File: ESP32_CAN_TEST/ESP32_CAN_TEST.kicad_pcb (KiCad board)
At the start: 2 copper layers, 45.7 x 45.7 mm, 56 parts, among them J1 XT60, J2 Encoder_1, J3 Molex_2x2, J4 Encoder2, J5 i2C, J6 UART, J7 GH1.25, J8 Jack-DC, Q1 2N7002, Q2 2N7002, Q3 2N7002, Q4 2N7002, Q5 2N7002, Q6 2N7002, SW1 EN, SW2 EN, U1 AMS1117, U2 ESP32-WROOM-32, U3 AOZ1282CI, U4 SN65HVD230

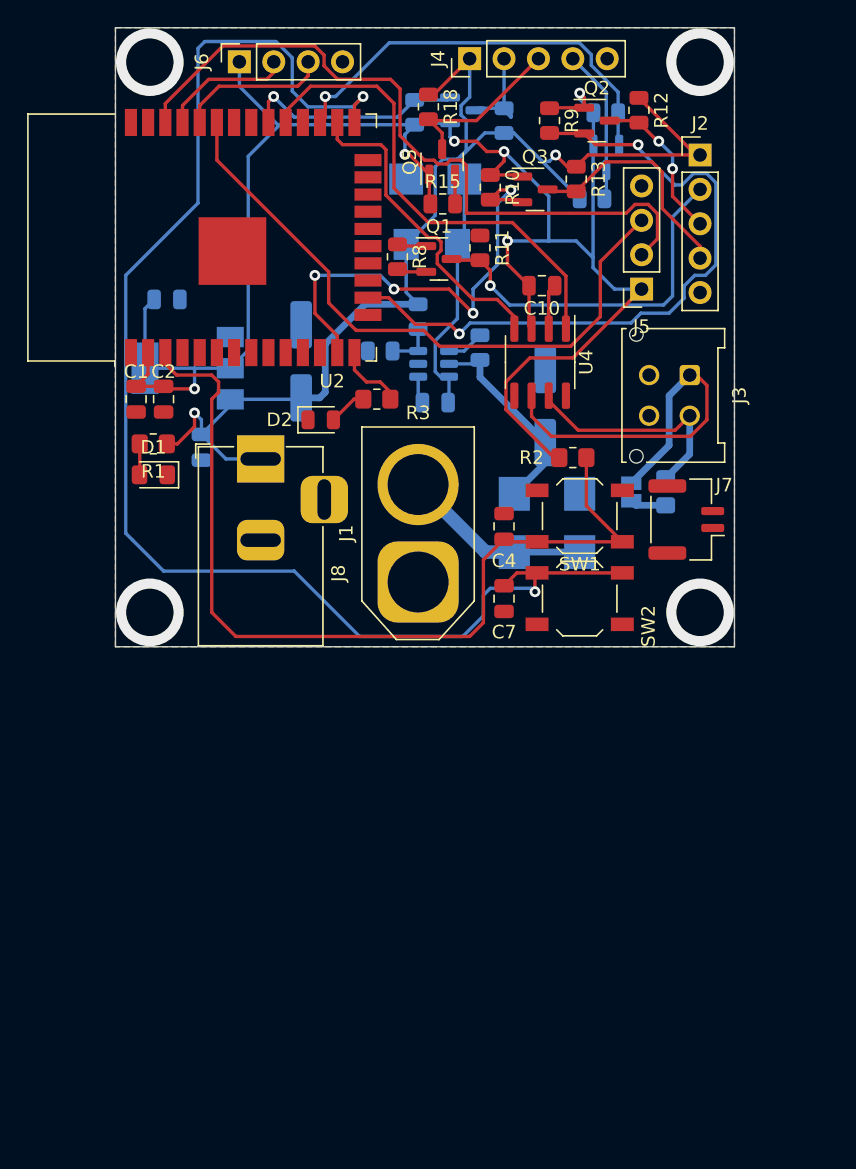
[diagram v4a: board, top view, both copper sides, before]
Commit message: esp32 fixed canbus
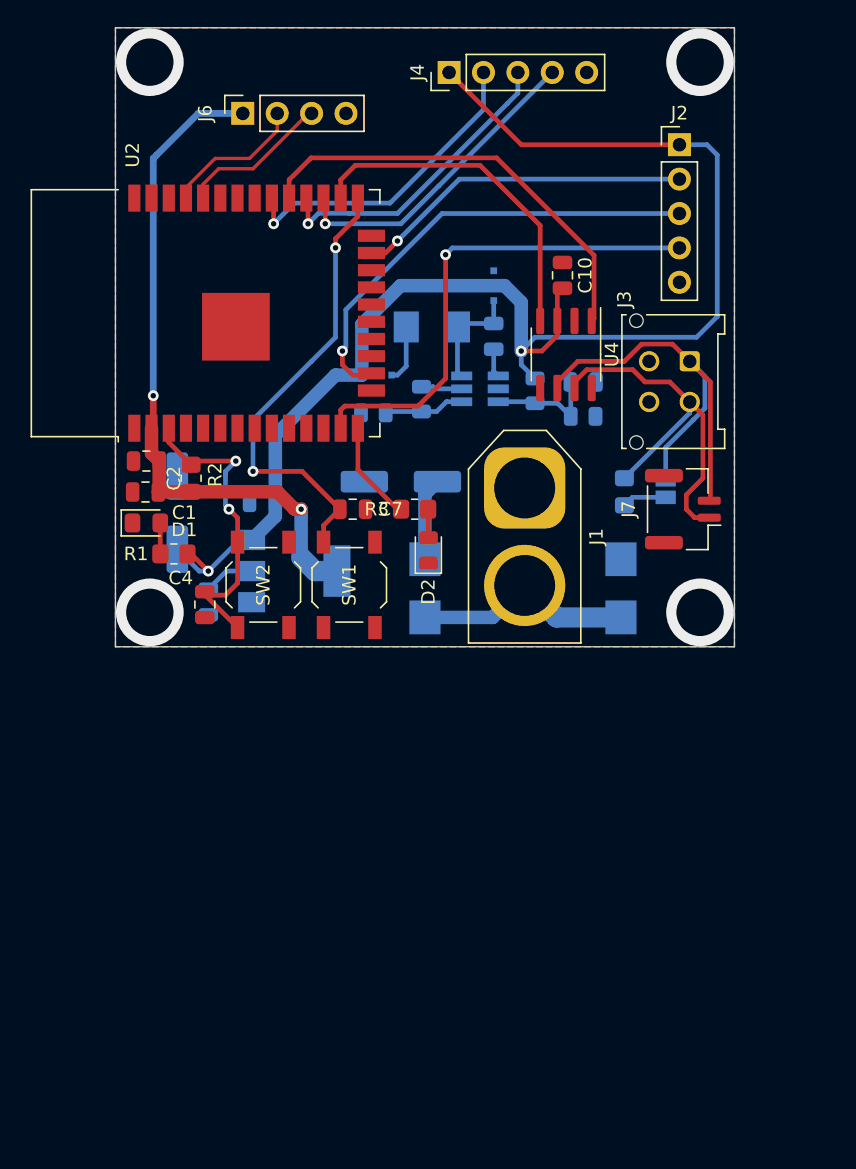
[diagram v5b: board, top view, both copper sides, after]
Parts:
- removed J5: i2C, Connector_PinSocket_2.54mm:PinSocket_1x04_P2.54mm_Vertical
- removed J8: Jack-DC, Connector_BarrelJack:BarrelJack_Horizontal
- removed Q1, Q2, Q3, Q4, Q5, Q6: 2N7002, Package_TO_SOT_SMD:SOT-23
- removed R10, R11, R12, R13, R14, R15, R16, R17, R18, R19, R9: 10K, Resistor_SMD:R_0805_2012Metric
- added C11: 100pF, Capacitor_SMD:C_0805_2012Metric, B.Cu at (136.1, 66.8)
- added D6: S4, Diode_SMD:D_SOD-323F, B.Cu at (129.5, 59.7)
- D5: value SS34 -> S4; footprint Diode_SMD:D_SMB -> Diode_SMD:D_SOD-323F
- L1: value 22uH -> 3.3uH
- R5: value 300K -> 27K
- R6: value 5.1k -> 22k
- R7: value 27K -> 124K
- R8: value 10K -> 2K2; moved to B.Cu
- U3: value AOZ1282CI -> MP2451; footprint Package_TO_SOT_SMD:SOT-23-6 -> Package_TO_SOT_SMD:SOT-23-6_Handsoldering
- U4: value SN65HVD230 -> TJA1051T
- moved R2 28.2 mm to (107.2, 73.9), turned to 90 degrees
- moved SW1 23.9 mm to (112.5, 81.8), turned to -90 degrees
- moved C4 22.8 mm to (108.2, 83.2), turned to -90 degrees
- moved C5 22.6 mm to (108.5, 83.1), turned to -90 degrees
- moved SW2 17.0 mm to (118.9, 81.8), turned to 90 degrees
- moved U1 16.9 mm to (114.8, 80.8), turned to 0 degrees
- moved R6 15.7 mm to (136.1, 69.3), turned to 0 degrees
- moved D5 15.1 mm to (120.9, 66.3), turned to 0 degrees
- moved C9 14.4 mm to (106.2, 76.5)
- moved C7 13.0 mm to (119.1, 76.2), turned to 180 degrees
- moved D2 12.5 mm to (124.7, 79.2), turned to 90 degrees
- moved C6 12.0 mm to (122.7, 74.2), turned to 180 degrees
- moved R8 11.7 mm to (120.7, 69.1), turned to 180 degrees
- moved J1 10.5 mm to (131.8, 74.6), turned to -90 degrees
- moved R7 10.2 mm to (132.6, 67.5)
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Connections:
- C10 pad 2: +3V3 -> +5V
- D5 pad 1: Net-(C8-Pad2) -> +5V
- D5 pad 2: GND -> Net-(L1-Pad2)
- J2 pad 2: Net-(J2-Pad2) -> /IO15
- J2 pad 3: Net-(J2-Pad3) -> /IO13
- J2 pad 4: Net-(J2-Pad4) -> /IO14
- J4 pad 2: Net-(J4-Pad2) -> /IO18
- J4 pad 3: Net-(J4-Pad3) -> /IO17
- J4 pad 4: Net-(J4-Pad4) -> /IO16
- L1 pad 2: +5V -> Net-(L1-Pad2)
- R8 pad 1: +3V3 -> Net-(R5-Pad2)
- R8 pad 2: /IO15 -> GND
- U4 pad 3: +3V3 -> +5V
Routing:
- net +3V3: track 141.5 -> 54.5 mm, vias 6 -> 2
- net Net-(C7-Pad2): track 102.8 -> 33.9 mm
- net /SCL: track 53.5 -> 0.00 mm
- net /SDA: track 47.4 -> 0.00 mm
- net Net-(C4-Pad1): track 66.7 -> 23.2 mm, vias 0 -> 2
- net Net-(J2-Pad2): track 27.4 -> 0.00 mm, vias 1 -> 0
- net /IO15: track 2.21 -> 25.0 mm, vias 0 -> 1
- net /IO17: track 2.17 -> 23.0 mm, vias 0 -> 1
- net +5V: track 89.0 -> 106.3 mm
- net Net-(J2-Pad4): track 17.2 -> 0.00 mm
- net /IO13: track 50.2 -> 34.3 mm, vias 2 -> 1
- net Net-(J4-Pad3): track 12.0 -> 0.00 mm
- net Net-(J2-Pad3): track 11.6 -> 0.00 mm, vias 2 -> 0
- net Net-(J4-Pad4): track 11.4 -> 0.00 mm
- net /CANL-: track 17.5 -> 28.7 mm
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
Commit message: esp32 fixed canbus
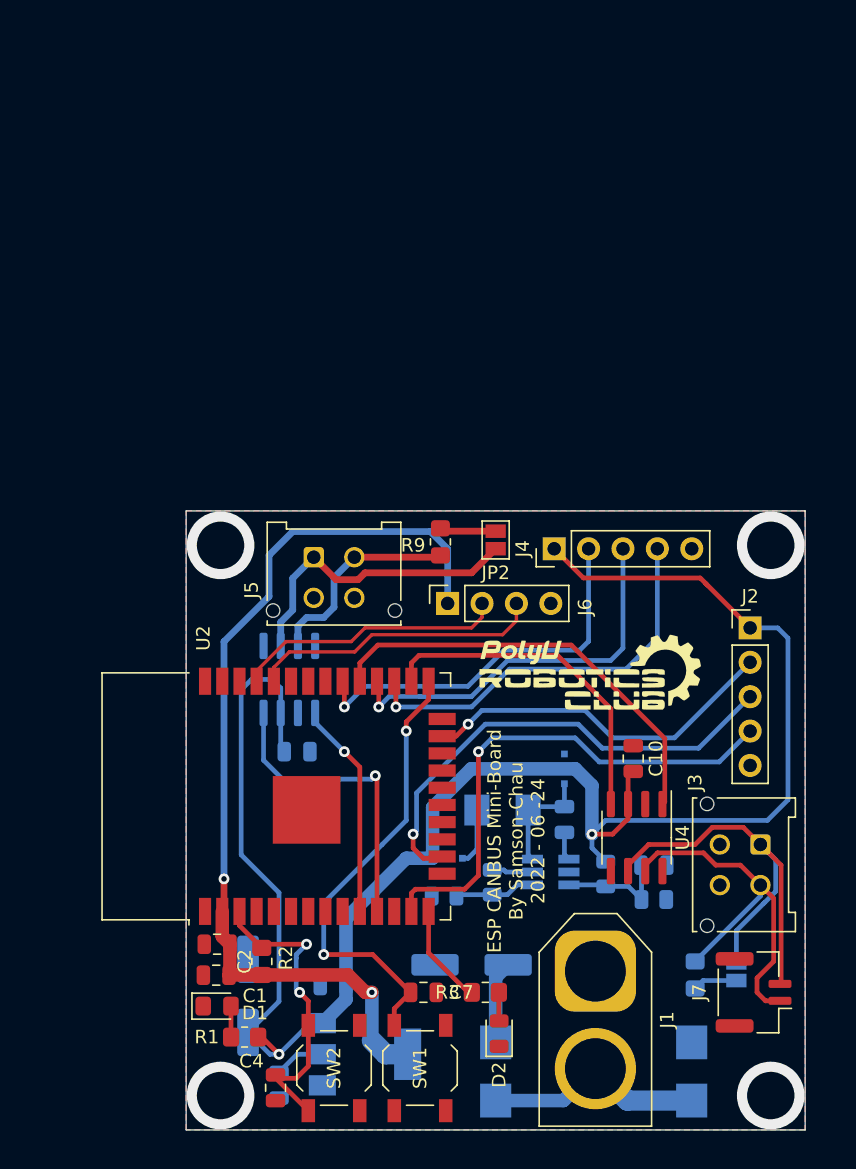
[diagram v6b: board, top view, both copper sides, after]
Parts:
- added C12: 0.1u, Capacitor_SMD:C_0805_2012Metric, B.Cu at (115.0, 94.1)
- added G***: LOGO, PolyuRobotics:Club_logo, F.Cu at (136.8, 88.5)
- added J5: Molex_2x2, Connector_Molex:Molex_Micro-Fit_3.0_43045-0412_2x02_P3.00mm_Vertical, F.Cu at (116.2, 79.7)
- added JP2: Jumper, Jumper:SolderJumper-2_P1.3mm_Open_Pad1.0x1.5mm, F.Cu at (129.7, 78.5)
- added R9: 120R, Resistor_SMD:R_0805_2012Metric_Pad1.20x1.40mm_HandSolder, F.Cu at (125.6, 78.6)
- added U5: TJA1051T, Package_SO:SOIC-8_3.9x4.9mm_P1.27mm, B.Cu at (114.4, 88.8)
- moved J6 39.2 mm to (126.1, 83.2)
- moved C4 36.1 mm to (113.4, 118.9)
- moved C3 36.1 mm to (117.7, 111.4)
- moved C9 36.1 mm to (111.4, 112.1)
- moved D1 36.1 mm to (109.1, 112.9)
- moved J2 36.1 mm to (148.5, 85.0)
- moved R8 36.1 mm to (125.9, 104.8)
- moved C1 36.1 mm to (109.0, 110.6)
- moved C8 36.1 mm to (134.8, 99.1)
- moved D2 36.1 mm to (129.9, 114.9)
- moved D3 36.1 mm to (144.2, 117.7)
- moved D6 36.1 mm to (134.8, 95.4)
- moved J1 36.1 mm to (137.0, 110.3)
- moved J3 36.1 mm to (149.2, 101.0)
- moved J7 36.1 mm to (148.7, 111.9)
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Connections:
- U2 pad 10: /IO25 -> /CAN2_TX
- U2 pad 11: /IO26 -> /CAN2_RX
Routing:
- net +5V: track 106.3 -> 139.9 mm
- net /CAN2H+: track 0.00 -> 22.6 mm
- net /CAN2_RX: track 0.00 -> 22.5 mm, vias 0 -> 1
- net +3V3: track 54.5 -> 72.8 mm
- net /CAN2_TX: track 0.00 -> 16.0 mm, vias 0 -> 1
- net /CAN2L-: track 0.00 -> 15.4 mm
- net /RXD: track 11.2 -> 21.7 mm
- net /TXD: track 10.5 -> 20.1 mm
- net /IO16: track 23.3 -> 30.0 mm
- net /IO17: track 23.0 -> 29.1 mm
- net /IO18: track 23.7 -> 28.8 mm
- net Net-(JP2-Pad2): track 0.00 -> 4.17 mm
- net /IO15: track 25.0 -> 26.7 mm
- net /IO14: track 36.7 -> 38.2 mm
- net /IO13: track 34.3 -> 35.7 mm
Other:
- board text added: "ESP CANBUS Mini-Board By Samson-Chau 2022 - 06 -24"

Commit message: ESP Board Update
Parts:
- moved R8 7.06 mm to (132.8, 105.9), turned to 0 degrees
- moved D5 2.91 mm to (127.8, 99.6), turned to 90 degrees
- moved U4 2.69 mm to (137.4, 100.6)
- moved C10 2.56 mm to (141.2, 96.8)
- moved L1 2.21 mm to (131.3, 96.5), turned to 90 degrees
- moved U1 1.40 mm to (119.9, 117.9)
- moved D6 0.63 mm to (135.4, 95.5)
- moved R5 0.63 mm to (129.0, 104.2)
- moved C12 0.38 mm to (115.0, 93.7)
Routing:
- net GND: track 0.00 -> 17.8 mm, vias 0 -> 39
- net Net-(C6-Pad1): track 9.14 -> 20.0 mm
- net +5V: track 139.9 -> 149.8 mm
- net Net-(C7-Pad2): track 33.9 -> 41.8 mm
- net +3V3: track 72.8 -> 79.1 mm
- net /CANH+: track 33.3 -> 36.5 mm
- net /CANL-: track 28.7 -> 31.8 mm
- net /IO13: track 35.7 -> 38.6 mm
- net /IO15: track 26.7 -> 25.0 mm
- net /IO18: track 28.8 -> 30.0 mm
- net /CAN_TX: track 32.2 -> 31.1 mm
- net Net-(D5-Pad2): track 4.25 -> 5.31 mm
- net /IO16: track 30.0 -> 28.9 mm
- net /CAN_RX: track 25.0 -> 24.0 mm
- net /IO17: track 29.1 -> 28.2 mm
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
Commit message: sad
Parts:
- removed C11: 100pF, Capacitor_SMD:C_0805_2012Metric
- removed C8: 100nF, Capacitor_SMD:C_0805_2012Metric
- removed D5, D6: S4, Diode_SMD:D_SOD-323F
- removed G***: LOGO, PolyuRobotics:Club_logo
- removed L1: 3.3uH, Inductor_SMD:L_Vishay_IHLP-1616
- removed R5: 27K, Resistor_SMD:R_0805_2012Metric
- removed R6: 22k, Resistor_SMD:R_0805_2012Metric
- removed R7: 124K, Resistor_SMD:R_0805_2012Metric
- removed R8: 2K2, Resistor_SMD:R_0805_2012Metric
- D1, JP2, R1, R9: moved to B.Cu
- JP1, R4: moved to F.Cu
- U3: value MP2451 -> MP1584; footprint Package_TO_SOT_SMD:SOT-23-6_Handsoldering -> PolyuRobotics:DC-DC-mp1584_module
- moved J4 41.9 mm to (144.0, 119.8), turned to -90 degrees
- moved C5 36.3 mm to (109.2, 82.7), turned to 0 degrees
- moved D1 34.6 mm to (114.3, 78.7), turned to 180 degrees
- moved R1 34.1 mm to (114.3, 81.3)
- moved J5 33.8 mm to (149.5, 85.8), turned to -90 degrees
- moved C1 33.2 mm to (116.3, 78.2)
- moved SW1 32.5 mm to (111.5, 85.6), turned to 180 degrees
- moved C9 31.4 mm to (140.1, 99.3), turned to -90 degrees
- moved U1 31.2 mm to (111.7, 87.8), turned to 180 degrees
- moved C4 30.8 mm to (117.1, 88.4)
- moved D3 29.4 mm to (114.7, 118.4)
- moved C2 28.5 mm to (116.3, 80.8)
- moved SW2 28.4 mm to (111.5, 92.0), turned to 0 degrees
- moved J1 26.5 mm to (111.5, 103.1)
- moved C12 25.8 mm to (140.8, 92.2)
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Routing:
- net +5V: track 149.8 -> 0.00 mm, vias 2 -> 0
- net +3V3: track 79.1 -> 0.00 mm, vias 2 -> 0
- net Net-(C7-Pad2): track 41.8 -> 0.35 mm, vias 2 -> 0
- net /IO14: track 38.9 -> 0.00 mm, vias 1 -> 0
- net /IO13: track 38.6 -> 0.00 mm, vias 1 -> 0
- net /CANH+: track 36.5 -> 5.09 mm
- net /CAN_TX: track 31.1 -> 0.00 mm
- net /IO18: track 30.0 -> 0.00 mm, vias 1 -> 0
- net /IO16: track 28.9 -> 0.00 mm, vias 1 -> 0
- net /IO17: track 28.2 -> 0.00 mm, vias 1 -> 0
- net /CANL-: track 31.8 -> 4.33 mm
- net /IO15: track 25.0 -> 0.00 mm, vias 1 -> 0
- net /CAN_RX: track 24.0 -> 0.00 mm
- net /CAN2_RX: track 22.7 -> 0.00 mm, vias 1 -> 0
- net /CAN2H+: track 22.6 -> 0.00 mm
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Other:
- board size 45.7 x 45.7 mm -> 45.8 x 45.8 mm
- board text removed: "ESP CANBUS Mini-Board By Samson-Chau 2022 - 06 -24"
